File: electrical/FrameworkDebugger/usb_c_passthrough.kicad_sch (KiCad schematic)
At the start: 15 parts, among them J2 USB_C_Receptacle, P1 USB_C_Plug, Q1 2N7002, Q2 2N7002, U1 NE5532

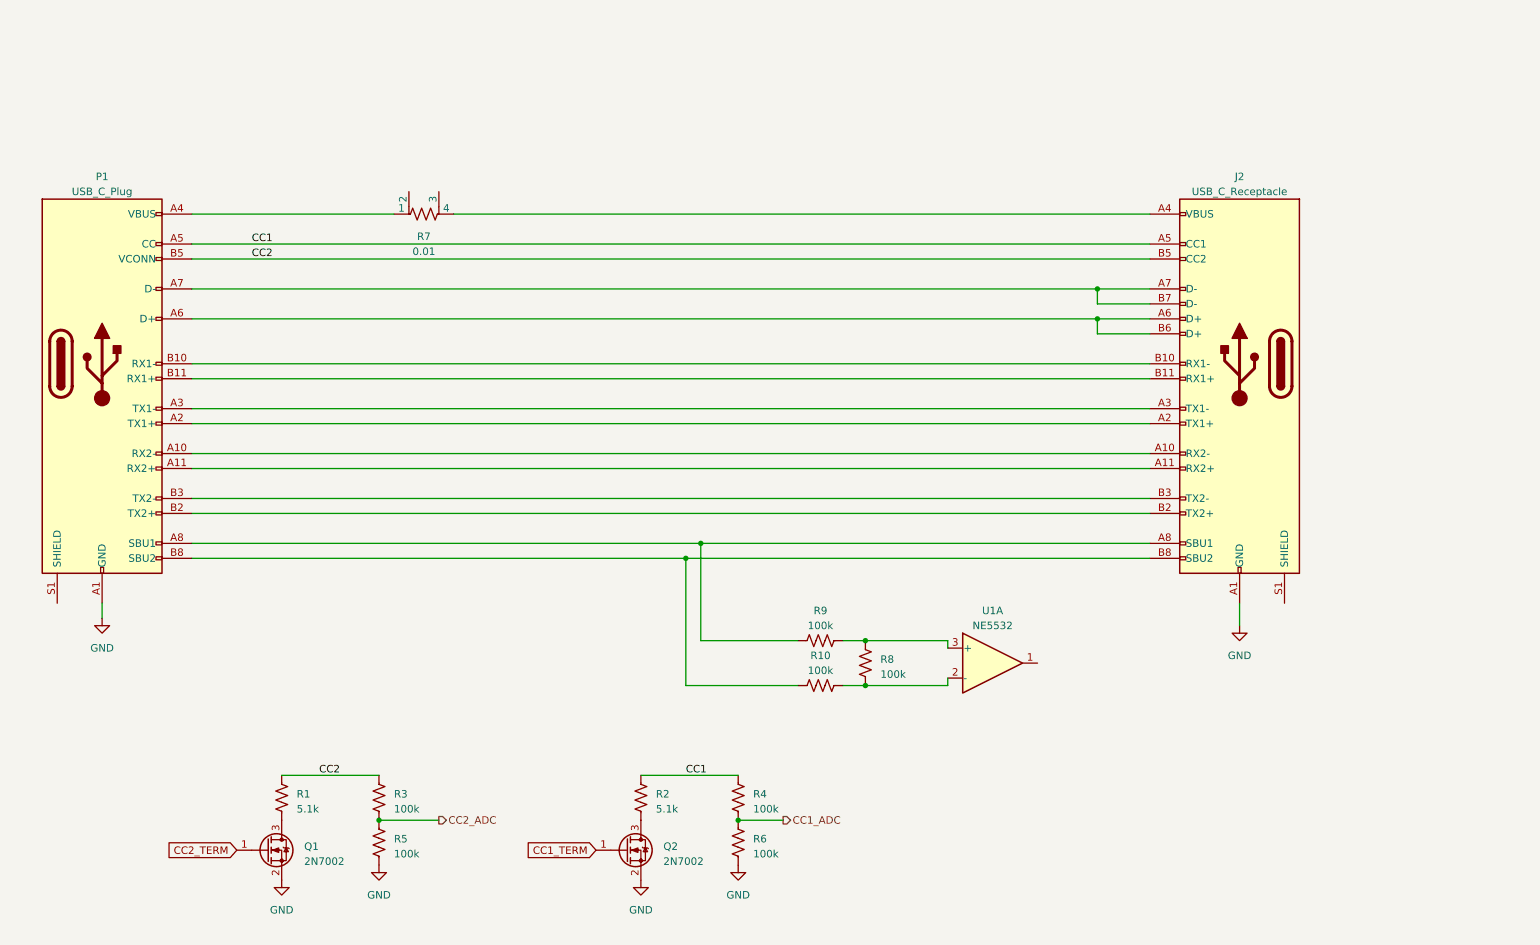
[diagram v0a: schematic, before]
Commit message: update design with rp2040
add type-c passthrough debug functionality
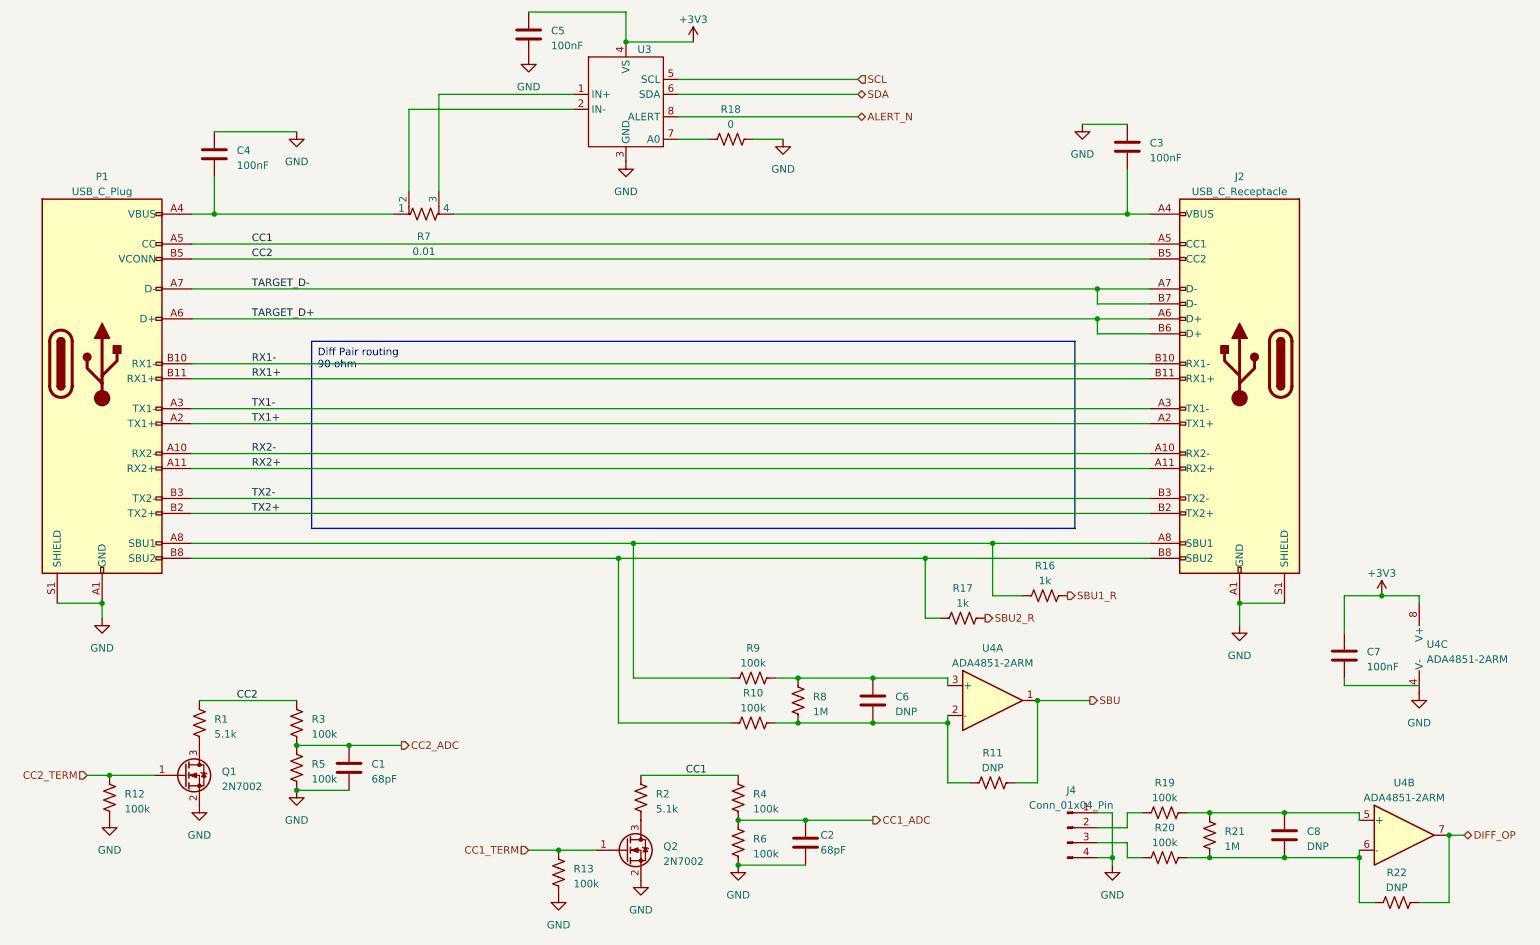
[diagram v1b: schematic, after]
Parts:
- removed U1: NE5532, symbol Amplifier_Operational:NE5532
- added C1, C2: 68pF, Capacitor_SMD:C_0402_1005Metric, symbol Device:C
- added C3, C4, C5, C7: 100nF, Capacitor_SMD:C_0402_1005Metric, symbol Device:C
- added C6, C8: DNP, Capacitor_SMD:C_0402_1005Metric, symbol Device:C
- added J4: Conn_01x04_Pin, Connector_PinHeader_2.54mm:PinHeader_1x04_P2.54mm_Vertical, symbol Connector:Conn_01x04_Pin
- added R11, R22: DNP, Resistor_SMD:R_0402_1005Metric, symbol Device:R_US
- added R12, R13, R19, R20: 100k, Resistor_SMD:R_0402_1005Metric, symbol Device:R_US
- added R16, R17: 1k, Resistor_SMD:R_0402_1005Metric, symbol Device:R_US
- added R18: 0, Resistor_SMD:R_0402_1005Metric, symbol Device:R_US
- added R21: 1M, Resistor_SMD:R_0402_1005Metric, symbol Device:R_US
- added U3: ~, Package_TO_SOT_SMD:SOT-23-8, symbol INA236:INA236
- added U4: ADA4851-2ARM, Package_SO:MSOP-8_3x3mm_P0.65mm, symbol Amplifier_Operational:ADA4807-2ARM
- P1: footprint (none) -> Connector_USB:USB_C_Plug_Molex_105444
- R1, R10, R2, R3, R4, R5, R6, R9: footprint Resistor_SMD:R_0805_2012Metric -> Resistor_SMD:R_0402_1005Metric
- R8: value 100k -> 1M; footprint Resistor_SMD:R_0805_2012Metric -> Resistor_SMD:R_0402_1005Metric
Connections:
- net CC1_ADC: now also C2.1
- net CC1_TERM: now also R13.1
- net CC2_ADC: now also C1.1
- net CC2_TERM: now also R12.1
- net GND: now also J2.S1 (SHIELD), P1.S1 (SHIELD), C1.2, C2.2, C3.1, C4.1, C5.2, J4.1 (Pin_1), J4.4 (Pin_4), R12.2, R13.2, R18.1, U3.3 (GND), U4.4 (V-)
- net at J2.B8 (SBU2), P1.B8 (SBU2), R10.1: now also R17.1
- net at R10.2, R8.2: now also C6.2, R11.1, U4.2 (-)
- net at P1.A4 (VBUS), P1.A9 (VBUS), P1.B4 (VBUS)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: now also C4.2
- net at R7.2: now also U3.2 (IN-)
- net at R7.3: now also U3.1 (IN+)
- net at J2.A4 (VBUS), J2.A9 (VBUS), J2.B4 (VBUS)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: now also C3.2
- net at J2.A8 (SBU1), P1.A8 (SBU1), R9.1: now also R16.1
- net at R8.1, R9.2: now also C6.1, U4.3 (+)
- net RX2-: now reaches J2.A10 (RX2-), P1.A10 (RX2-)
- net RX2+: now reaches J2.A11 (RX2+), P1.A11 (RX2+)
- net TX1+: now reaches J2.A2 (TX1+), P1.A2 (TX1+)
- net TX1-: now reaches J2.A3 (TX1-), P1.A3 (TX1-)
- net TARGET_D+: now reaches J2.A6 (D+), J2.B6 (D+), P1.A6 (D+)
- net TARGET_D-: now reaches J2.A7 (D-), J2.B7 (D-), P1.A7 (D-)
- net RX1-: now reaches J2.B10 (RX1-), P1.B10 (RX1-)
- net RX1+: now reaches J2.B11 (RX1+), P1.B11 (RX1+)
- net TX2+: now reaches J2.B2 (TX2+), P1.B2 (TX2+)
- net TX2-: now reaches J2.B3 (TX2-), P1.B3 (TX2-)
- new net: R18.2, U3.7 (A0)
- new net: C8.2, R20.2, R21.2, R22.1, U4.6 (-)
- new net: C8.1, R19.2, R21.1, U4.5 (+)
- new net: J4.2 (Pin_2), R19.1
- new net: J4.3 (Pin_3), R20.1
- new net +3V3: C5.1, C7.1, U3.4 (VS), U4.8 (V+)
- new net ALERT_N: U3.8 (ALERT)
- new net DIFF_OP: R22.2, U4.7
- new net SBU: R11.2, U4.1
- new net SBU1_R: R16.2
- new net SBU2_R: R17.2
- new net SCL: U3.5 (SCL)
- new net SDA: U3.6 (SDA)
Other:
- moved on the sheet: Q1, R1, R10, R3, R5, R8, R9
